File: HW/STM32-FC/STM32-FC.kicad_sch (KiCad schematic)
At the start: 38 parts, among them J1 GH 1.25mm 6P, Q1 S9013, SW2 SW_DIP_x03, U1 STM32F407VETx, Y1 16MHz

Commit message: 2025.02.01 PCB Routing start
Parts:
- D1: value Red -> White; footprint LED_SMD:LED_0603_1608Metric -> LED_SMD:LED_0402_1005Metric
- D2, D4, D5: footprint LED_SMD:LED_0603_1608Metric -> LED_SMD:LED_0402_1005Metric

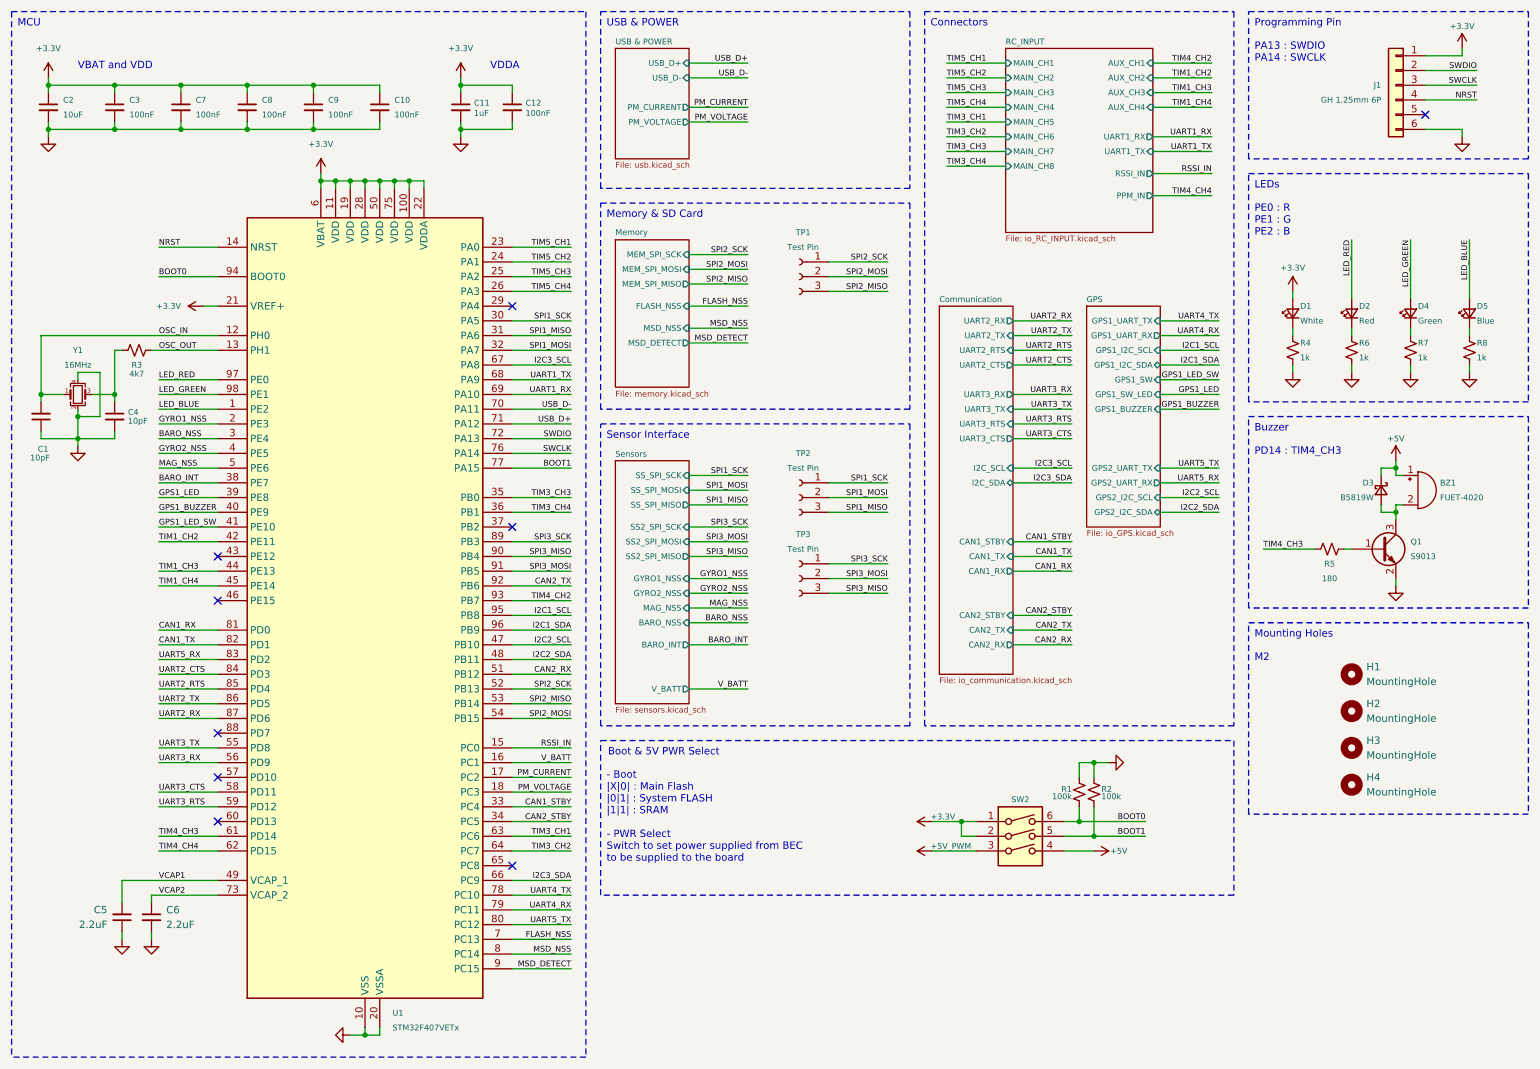
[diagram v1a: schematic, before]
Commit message: 2025.02.01 PCB routing update 1
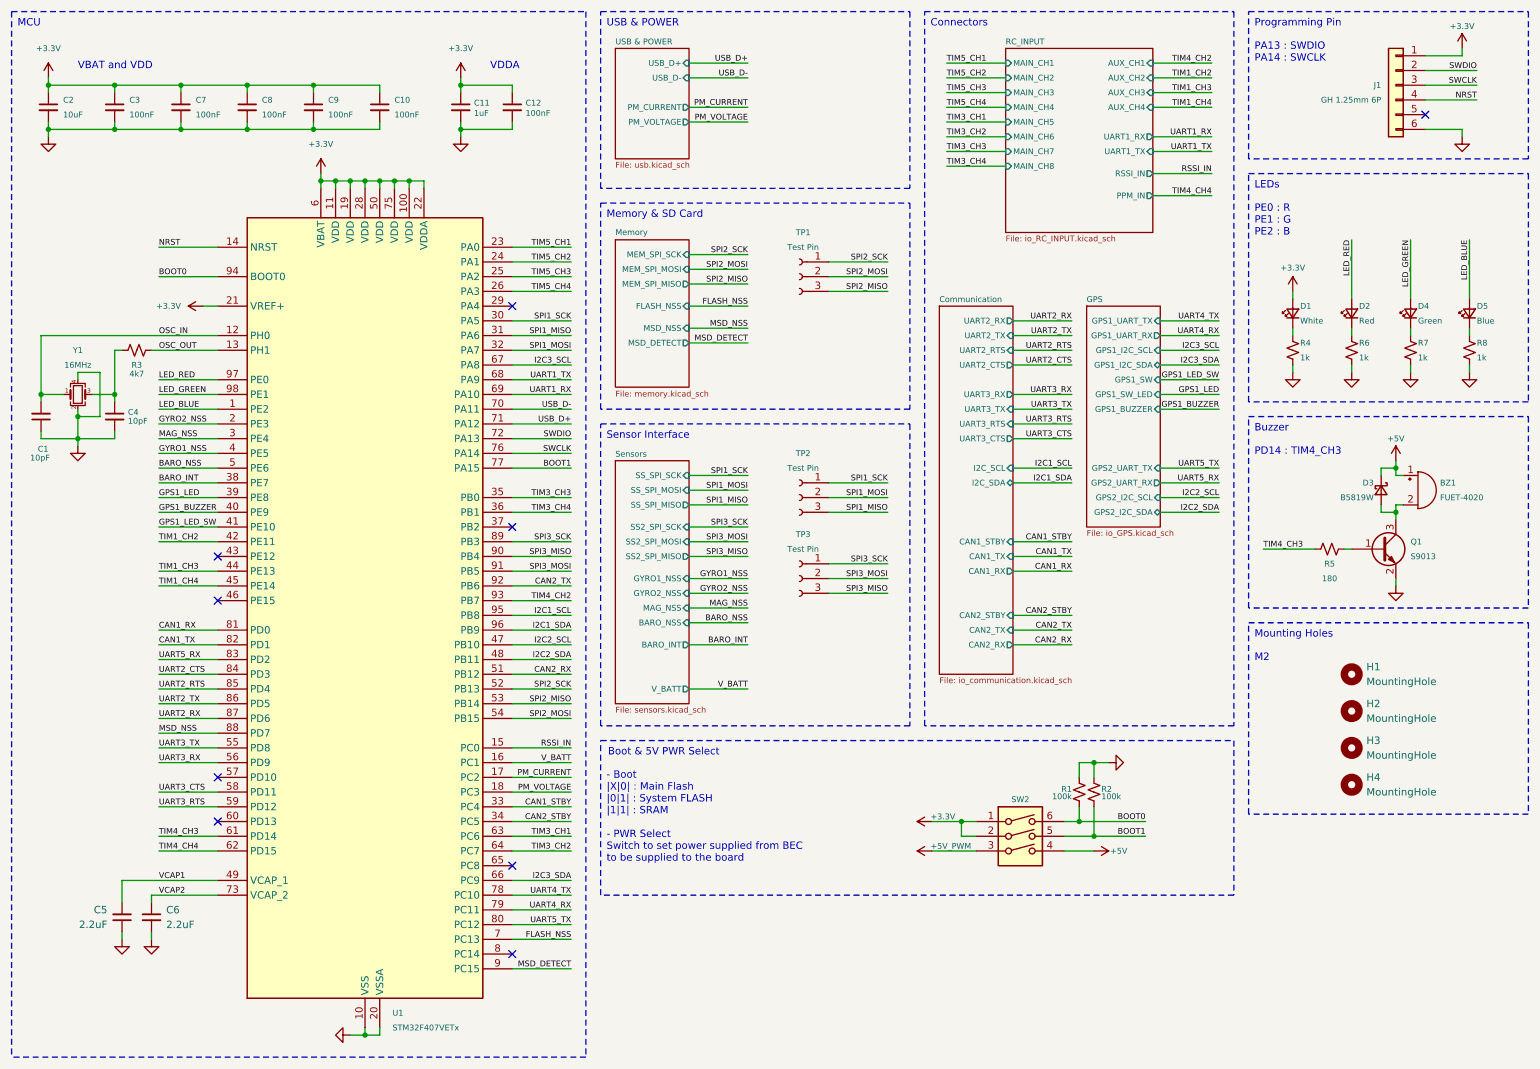
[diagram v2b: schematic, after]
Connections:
- net BARO_NSS: now also U1.5 (PE6); no longer U1.3 (PE4)
- net GYRO1_NSS: now also U1.4 (PE5); no longer U1.2 (PE3)
- net GYRO2_NSS: now also U1.2 (PE3); no longer U1.4 (PE5)
- net MAG_NSS: now also U1.3 (PE4); no longer U1.5 (PE6)
- net MSD_NSS: now also U1.88 (PD7); no longer U1.8 (PC14)
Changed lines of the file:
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@@
 	)
 	(no_connect
-		(at 58.42 137.16)
+		(at 266.7 30.48)
 	)
 	(no_connect
-		(at 266.7 30.48)
+		(at 109.22 175.26)
 	)
 	(no_connect
@@
 	(wire
 		(pts
-			(xy 220.98 73.66) (xy 231.14 73.66)
+			(xy 195.58 93.98) (xy 205.74 93.98)
 		)
 		(stroke
@@
 	(wire
 		(pts
-			(xy 195.58 91.44) (xy 205.74 91.44)
+			(xy 220.98 71.12) (xy 231.14 71.12)
 		)
 		(stroke
@@
 	(wire
 		(pts
-			(xy 220.98 71.12) (xy 231.14 71.12)
+			(xy 195.58 91.44) (xy 205.74 91.44)
 		)
 		(stroke
@@
 	(wire
 		(pts
+			(xy 58.42 83.82) (xy 48.26 83.82)
+		)
+		(stroke
+			(width 0)
+			(type default)
+		)
+	)
+	(wire
+		(pts
 			(xy 58.42 88.9) (xy 48.26 88.9)
 		)
@@
 	(wire
 		(pts
-			(xy 58.42 83.82) (xy 48.26 83.82)
-		)
-		(stroke
-			(width 0)
-			(type default)
-		)
-	)
-	(wire
-		(pts
 			(xy 273.05 33.02) (xy 273.05 34.29)
 		)
@@
 	(wire
 		(pts
-			(xy 58.42 86.36) (xy 48.26 86.36)
+			(xy 58.42 91.44) (xy 48.26 91.44)
 		)
 		(stroke
@@
 	(wire
 		(pts
-			(xy 58.42 91.44) (xy 48.26 91.44)
+			(xy 58.42 86.36) (xy 48.26 86.36)
 		)
 		(stroke
@@
 	(wire
 		(pts
-			(xy 109.22 175.26) (xy 119.38 175.26)
+			(xy 58.42 137.16) (xy 48.26 137.16)
 		)
 		(stroke
@@
 	(wire
 		(pts
-			(xy 195.58 93.98) (xy 205.74 93.98)
+			(xy 220.98 73.66) (xy 231.14 73.66)
 		)
 		(stroke
@@
 	)
 	(label "I2C1_SCL"
-		(at 231.14 71.12 180)
+		(at 205.74 91.44 180)
 		(effects
 			(font
@@
 		)
 	)
-	(label "GYRO1_NSS"
-		(at 48.26 83.82 0)
-		(effects
-			(font
-				(size 1 1)
-			)
-			(justify left bottom)
-		)
-	)
 	(label "VCAP1"
 		(at 48.26 162.56 0)
@@
 	)
 	(label "I2C3_SDA"
-		(at 205.74 93.98 180)
+		(at 231.14 73.66 180)
 		(effects
 			(font
@@
 		)
 	)
+	(label "GYRO1_NSS"
+		(at 48.26 88.9 0)
+		(effects
+			(font
+				(size 1 1)
+			)
+			(justify left bottom)
+		)
+	)
 	(label "SPI3_SCK"
 		(at 119.38 104.14 180)
@@
 	)
 	(label "MAG_NSS"
-		(at 48.26 91.44 0)
+		(at 48.26 86.36 0)
 		(effects
 			(font
@@
 	)
 	(label "BARO_NSS"
-		(at 48.26 86.36 0)
+		(at 48.26 91.44 0)
 		(effects
 			(font
@@
 	)
 	(label "GYRO2_NSS"
-		(at 48.26 88.9 0)
+		(at 48.26 83.82 0)
 		(effects
 			(font
@@
 	)
 	(label "I2C1_SDA"
-		(at 231.14 73.66 180)
+		(at 205.74 93.98 180)
 		(effects
 			(font
@@
 	)
 	(label "I2C3_SCL"
-		(at 205.74 91.44 180)
+		(at 231.14 71.12 180)
 		(effects
 			(font
@@
 	)
 	(label "MSD_NSS"
-		(at 119.38 175.26 180)
+		(at 48.26 137.16 0)
 		(effects
 			(font
 				(size 1 1)
 			)
-			(justify right bottom)
+			(justify left bottom)
 		)
 	)

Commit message: 2025.02.03 PCB routing update 2
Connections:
- net +3.3V: now also SW2.3; no longer SW2.1
- net +5V: now also SW2.6; no longer SW2.4
- net +5V_PWM: now also SW2.1; no longer SW2.3
- net BOOT0: now also SW2.4; no longer SW2.6
- net SPI1_MISO: now also TP2.2 (Pin_2); no longer TP2.3 (Pin_3)
- net SPI1_MOSI: now also TP2.3 (Pin_3); no longer TP2.2 (Pin_2)
- net SPI2_MISO: now also TP1.2 (Pin_2); no longer TP1.3 (Pin_3)
- net SPI2_MOSI: now also TP1.3 (Pin_3); no longer TP1.2 (Pin_2)
- net SPI3_MISO: now also TP3.2 (Pin_2); no longer TP3.3 (Pin_3)
- net SPI3_MOSI: now also TP3.3 (Pin_3); no longer TP3.2 (Pin_2)
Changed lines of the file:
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@@
 	(wire
 		(pts
-			(xy 194.31 31.75) (xy 184.15 31.75)
+			(xy 194.31 26.67) (xy 184.15 26.67)
 		)
 		(stroke
@@
 	(wire
 		(pts
-			(xy 194.31 24.13) (xy 184.15 24.13)
+			(xy 194.31 34.29) (xy 184.15 34.29)
 		)
 		(stroke
@@
 	(wire
 		(pts
-			(xy 194.31 21.59) (xy 184.15 21.59)
+			(xy 194.31 31.75) (xy 184.15 31.75)
 		)
 		(stroke
@@
 	(wire
 		(pts
-			(xy 163.83 60.96) (xy 173.99 60.96)
+			(xy 163.83 58.42) (xy 173.99 58.42)
 		)
 		(stroke
@@
 	(wire
 		(pts
-			(xy 229.87 44.45) (xy 219.71 44.45)
+			(xy 139.7 69.85) (xy 149.86 69.85)
 		)
 		(stroke
@@
 	(wire
 		(pts
-			(xy 139.7 69.85) (xy 149.86 69.85)
+			(xy 261.62 97.79) (xy 261.62 99.06)
 		)
 		(stroke
@@
 	(wire
 		(pts
-			(xy 261.62 97.79) (xy 261.62 99.06)
+			(xy 195.58 106.68) (xy 205.74 106.68)
 		)
 		(stroke
@@
 	(wire
 		(pts
-			(xy 195.58 106.68) (xy 205.74 106.68)
+			(xy 93.98 43.18) (xy 93.98 41.91)
 		)
 		(stroke
@@
 	(wire
 		(pts
-			(xy 93.98 43.18) (xy 93.98 41.91)
+			(xy 195.58 119.38) (xy 205.74 119.38)
 		)
 		(stroke
@@
 	(wire
 		(pts
-			(xy 195.58 119.38) (xy 205.74 119.38)
+			(xy 219.71 44.45) (xy 229.87 44.45)
 		)
 		(stroke
@@
 	(wire
 		(pts
-			(xy 163.83 110.49) (xy 173.99 110.49)
+			(xy 163.83 113.03) (xy 173.99 113.03)
 		)
 		(stroke
@@
 	(wire
 		(pts
-			(xy 219.71 29.21) (xy 229.87 29.21)
-		)
-		(stroke
-			(width 0)
-			(type default)
-		)
-	)
-	(wire
-		(pts
 			(xy 275.59 25.4) (xy 266.7 25.4)
 		)
@@
 	(wire
 		(pts
-			(xy 194.31 29.21) (xy 184.15 29.21)
+			(xy 194.31 39.37) (xy 184.15 39.37)
 		)
 		(stroke
@@
 	(wire
 		(pts
-			(xy 163.83 58.42) (xy 173.99 58.42)
+			(xy 163.83 60.96) (xy 173.99 60.96)
 		)
 		(stroke
@@
 	(wire
 		(pts
-			(xy 194.31 34.29) (xy 184.15 34.29)
+			(xy 194.31 29.21) (xy 184.15 29.21)
 		)
 		(stroke
@@
 	(wire
 		(pts
-			(xy 163.83 96.52) (xy 173.99 96.52)
+			(xy 163.83 99.06) (xy 173.99 99.06)
 		)
 		(stroke
@@
 	(wire
 		(pts
-			(xy 194.31 39.37) (xy 184.15 39.37)
+			(xy 219.71 24.13) (xy 229.87 24.13)
 		)
 		(stroke
@@
 	(wire
 		(pts
+			(xy 184.15 24.13) (xy 194.31 24.13)
+		)
+		(stroke
+			(width 0)
+			(type default)
+		)
+	)
+	(wire
+		(pts
 			(xy 109.22 121.92) (xy 119.38 121.92)
 		)
@@
 	(wire
 		(pts
-			(xy 163.83 99.06) (xy 173.99 99.06)
+			(xy 163.83 96.52) (xy 173.99 96.52)
 		)
 		(stroke
@@
 	(wire
 		(pts
-			(xy 163.83 113.03) (xy 173.99 113.03)
+			(xy 163.83 110.49) (xy 173.99 110.49)
 		)
 		(stroke
@@
 	(wire
 		(pts
-			(xy 194.31 36.83) (xy 184.15 36.83)
+			(xy 219.71 21.59) (xy 229.87 21.59)
 		)
 		(stroke
@@
 	(wire
 		(pts
-			(xy 219.71 26.67) (xy 229.87 26.67)
+			(xy 219.71 29.21) (xy 229.87 29.21)
 		)
 		(stroke
@@
 	(wire
 		(pts
-			(xy 194.31 26.67) (xy 184.15 26.67)
+			(xy 194.31 36.83) (xy 184.15 36.83)
 		)
 		(stroke
@@
 	(wire
 		(pts
-			(xy 219.71 21.59) (xy 229.87 21.59)
+			(xy 194.31 21.59) (xy 184.15 21.59)
 		)
 		(stroke
@@
 	(wire
 		(pts
-			(xy 219.71 24.13) (xy 229.87 24.13)
+			(xy 219.71 26.67) (xy 229.87 26.67)
 		)
 		(stroke
@@
 	)
 	(label "TIM5_CH2"
-		(at 184.15 24.13 0)
+		(at 184.15 34.29 0)
 		(effects
 			(font
@@
 	)
 	(label "TIM1_CH2"
-		(at 229.87 24.13 180)
+		(at 229.87 26.67 180)
 		(effects
 			(font
@@
 	)
 	(label "SPI3_MOSI"
-		(at 173.99 110.49 180)
+		(at 173.99 113.03 180)
 		(effects
 			(font
@@
 		)
 	)
+	(label "TIM4_CH4"
+		(at 184.15 24.13 0)
+		(effects
+			(font
+				(size 1 1)
+			)
+			(justify left bottom)
+		)
+	)
 	(label "TIM4_CH2"
-		(at 229.87 21.59 180)
+		(at 184.15 21.59 0)
 		(effects
 			(font
 				(size 1 1)
 			)
-			(justify right bottom)
+			(justify left bottom)
 		)
 	)
@@
 	)
 	(label "TIM1_CH3"
-		(at 229.87 26.67 180)
+		(at 229.87 29.21 180)
 		(effects
 			(font
@@
 	)
 	(label "SPI2_MOSI"
-		(at 173.99 58.42 180)
+		(at 173.99 60.96 180)
 		(effects
 			(font
@@
 	)
 	(label "TIM5_CH3"
-		(at 184.15 26.67 0)
+		(at 184.15 36.83 0)
 		(effects
 			(font
@@
 	)
 	(label "TIM3_CH1"
-		(at 184.15 31.75 0)
+		(at 184.15 26.67 0)
 		(effects
 			(font
@@
 	)
 	(label "TIM3_CH2"
-		(at 184.15 34.29 0)
+		(at 184.15 29.21 0)
 		(effects
 			(font
@@
 	)
 	(label "SPI2_MISO"
-		(at 173.99 60.96 180)
+		(at 173.99 58.42 180)
 		(effects
 			(font
@@
 	)
 	(label "SPI1_MISO"
-		(at 173.99 99.06 180)
+		(at 173.99 96.52 180)
 		(effects
 			(font
@@
 	)
 	(label "TIM5_CH1"
-		(at 184.15 21.59 0)
+		(at 184.15 31.75 0)
 		(effects
 			(font
@@
 	)
 	(label "TIM5_CH4"
-		(at 184.15 29.21 0)
+		(at 184.15 39.37 0)
 		(effects
 			(font
@@
 	)
 	(label "TIM3_CH3"
-		(at 184.15 36.83 0)
+		(at 229.87 21.59 180)
 		(effects
 			(font
 				(size 1 1)
 			)
-			(justify left bottom)
+			(justify right bottom)
 		)
 	)
 	(label "TIM3_CH4"
-		(at 184.15 39.37 0)
+		(at 229.87 24.13 180)
 		(effects
 			(font
 				(size 1 1)
 			)
-			(justify left bottom)
+			(justify right bottom)
 		)
 	)
@@
 		)
 	)
-	(label "TIM4_CH4"
+	(label "TIM1_CH4"
 		(at 229.87 44.45 180)
 		(effects
@@
 	)
 	(label "SPI3_MISO"
-		(at 173.99 113.03 180)
+		(at 173.99 110.49 180)
 		(effects
 			(font
@@
 		)
 	)
-	(label "TIM1_CH4"
-		(at 229.87 29.21 180)
-		(effects
-			(font
-				(size 1 1)
-			)
-			(justify right bottom)
-		)
-	)
 	(label "CAN1_TX"
 		(at 205.74 106.68 180)
@@
 	)
 	(label "SPI1_MOSI"
-		(at 173.99 96.52 180)
+		(at 173.99 99.06 180)
 		(effects
 			(font
@@
 		(lib_id "Switch:SW_DIP_x03")
 		(at 196.85 154.94 0)
+		(mirror x)
 		(unit 1)
 		(exclude_from_sim no)
@@
 		(dnp no)
 		(property "Reference" "SW2"
-			(at 196.85 148.59 0)
+			(at 196.85 161.29 0)
 			(effects
 				(font
@@
 		)
 		(property "Value" "SW_DIP_x03"
-			(at 196.85 147.32 0)
+			(at 196.85 162.56 0)
 			(effects
 				(font
@@
 		)
 		(property "Footprint" "Button_Switch_SMD:SW_DIP_SPSTx03_Slide_KingTek_DSHP03TJ_W5.25mm_P1.27mm_JPin"
-			(at 196.85 157.48 0)
+			(at 196.85 152.4 0)
 			(effects
 				(font
@@
 		)
 		(property "Datasheet" "~"
-			(at 196.85 157.48 0)
+			(at 196.85 152.4 0)
 			(effects
 				(font

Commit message: 2025.02.05 PCB routing done
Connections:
- net GPS1_BUZZER: now also U1.65 (PC8); no longer U1.40 (PE9)
- net GPS1_LED: now also U1.60 (PD13); no longer U1.39 (PE8)
- net GPS1_LED_SW: now also U1.57 (PD10); no longer U1.41 (PE10)
- net RSSI_IN: now also U1.16 (PC1); no longer U1.15 (PC0)
- net V_BATT: now also U1.15 (PC0); no longer U1.16 (PC1)
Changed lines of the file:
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@@
 	(title_block
 		(title "STM32 Flight Controller")
-		(date "2025-01-03")
+		(date "2025-02-05")
 		(rev "A")
 		(company "NARAE")
@@
 	)
 	(no_connect
-		(at 109.22 160.02)
+		(at 58.42 96.52)
+	)
+	(no_connect
+		(at 58.42 99.06)
 	)
 	(no_connect
@@
 	)
 	(no_connect
-		(at 58.42 144.78)
-	)
-	(no_connect
-		(at 58.42 152.4)
+		(at 58.42 101.6)
 	)
 	(wire
@@
 	(wire
 		(pts
-			(xy 194.31 26.67) (xy 184.15 26.67)
+			(xy 194.31 24.13) (xy 184.15 24.13)
 		)
 		(stroke
@@
 	(wire
 		(pts
-			(xy 109.22 142.24) (xy 119.38 142.24)
+			(xy 109.22 139.7) (xy 119.38 139.7)
 		)
 		(stroke
@@
 	(wire
 		(pts
-			(xy 48.26 99.06) (xy 58.42 99.06)
+			(xy 119.38 160.02) (xy 109.22 160.02)
 		)
 		(stroke
@@
 	(wire
 		(pts
-			(xy 48.26 101.6) (xy 58.42 101.6)
+			(xy 48.26 144.78) (xy 58.42 144.78)
 		)
 		(stroke
@@
 	(wire
 		(pts
-			(xy 48.26 96.52) (xy 58.42 96.52)
+			(xy 48.26 152.4) (xy 58.42 152.4)
 		)
 		(stroke
@@
 	(wire
 		(pts
-			(xy 109.22 139.7) (xy 119.38 139.7)
+			(xy 109.22 142.24) (xy 119.38 142.24)
 		)
 		(stroke
@@
 	(wire
 		(pts
-			(xy 194.31 29.21) (xy 184.15 29.21)
+			(xy 194.31 26.67) (xy 184.15 26.67)
 		)
 		(stroke
@@
 	(wire
 		(pts
-			(xy 184.15 24.13) (xy 194.31 24.13)
+			(xy 184.15 29.21) (xy 194.31 29.21)
 		)
 		(stroke
@@
 	)
 	(label "TIM4_CH4"
-		(at 184.15 24.13 0)
+		(at 184.15 29.21 0)
 		(effects
 			(font
@@
 	)
 	(label "TIM3_CH1"
-		(at 184.15 26.67 0)
+		(at 184.15 24.13 0)
 		(effects
 			(font
@@
 	)
 	(label "TIM3_CH2"
-		(at 184.15 29.21 0)
+		(at 184.15 26.67 0)
 		(effects
 			(font
@@
 	)
 	(label "GPS1_LED_SW"
-		(at 48.26 101.6 0)
+		(at 48.26 144.78 0)
 		(effects
 			(font
@@
 	)
 	(label "V_BATT"
-		(at 119.38 142.24 180)
+		(at 119.38 139.7 180)
 		(effects
 			(font
@@
 	)
 	(label "RSSI_IN"
-		(at 119.38 139.7 180)
+		(at 119.38 142.24 180)
 		(effects
 			(font
@@
 	)
 	(label "GPS1_BUZZER"
-		(at 48.26 99.06 0)
+		(at 119.38 160.02 180)
 		(effects
 			(font
 				(size 1 1)
 			)
-			(justify left bottom)
+			(justify right bottom)
 		)
 	)
@@
 	)
 	(label "GPS1_LED"
-		(at 48.26 96.52 0)
+		(at 48.26 152.4 0)
 		(effects
 			(font

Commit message: 2025.02.06 PCB routing done v2
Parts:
- added C35: 100nF, Capacitor_SMD:C_0402_1005Metric, symbol Device:C_Small
- BZ1: LCSC (none) -> C391027
- C1, C4: LCSC (none) -> C1545
- C10, C12, C3, C7, C8, C9: LCSC C1525 -> C1581
- C11: LCSC C1525 -> C1926
- C2: LCSC C19702 -> C40894
- C5, C6: LCSC (none) -> C1950
- D1: LCSC (none) -> C130725
- D2: LCSC (none) -> C130719
- D3: LCSC (none) -> C22624
- D4: LCSC (none) -> C130723
- D5: LCSC (none) -> C130724
- J1: LCSC (none) -> C189892
- Q1: LCSC (none) -> C111269
- R1, R2: LCSC (none) -> C25741
- R3: LCSC (none) -> C25900
- R4, R6, R7, R8: LCSC (none) -> C11702
- R5: LCSC (none) -> C38941
- SW2: LCSC (none) -> C5123689
- TP1, TP2, TP3: LCSC (none) -> C24980
- U1: LCSC (none) -> C28730
- Y1: LCSC (none) -> C1985423
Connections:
- net +3.3V: now also J1.6 (Pin_6); no longer J1.1 (Pin_1)
- net BOOT1: now also U1.37 (PB2); no longer U1.77 (PA15)
- net GND: now also J1.1 (Pin_1), C35.2; no longer J1.6 (Pin_6)
- net NRST: now also J1.3 (Pin_3), C35.1; no longer J1.4 (Pin_4)
- net SWCLK: now also J1.4 (Pin_4); no longer J1.3 (Pin_3)
- net SWDIO: now also J1.5 (Pin_5); no longer J1.2 (Pin_2)
- net GPS1_LED renamed GPS1_SW
- net GPS1_LED_SW renamed GPS1_SW_LED
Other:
- moved on the sheet: J1

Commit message: 2025.02.06 PCB routing done v3
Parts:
- J1: footprint JST_GH:JST_GH_BM06B-GHS-TBT_06 -> JST_GH:JST_GH_SM06B-GHS-TB_06x1.25mm_Angled; LCSC C189892 -> C19626244
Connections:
- net +3.3V: now also J1.1 (Pin_1); no longer J1.6 (Pin_6)
- net GND: now also J1.6 (Pin_6); no longer J1.1 (Pin_1)
- net NRST: now also J1.4 (Pin_4); no longer J1.3 (Pin_3)
- net SWCLK: now also J1.3 (Pin_3); no longer J1.4 (Pin_4)
- net SWDIO: now also J1.2 (Pin_2); no longer J1.5 (Pin_5)
- net TIM4_CH3 renamed Buzzer
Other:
- moved on the sheet: J1
